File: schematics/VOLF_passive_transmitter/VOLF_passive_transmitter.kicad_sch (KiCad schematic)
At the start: 7 parts, among them J1 AudioJack3, Q1 IRF3205

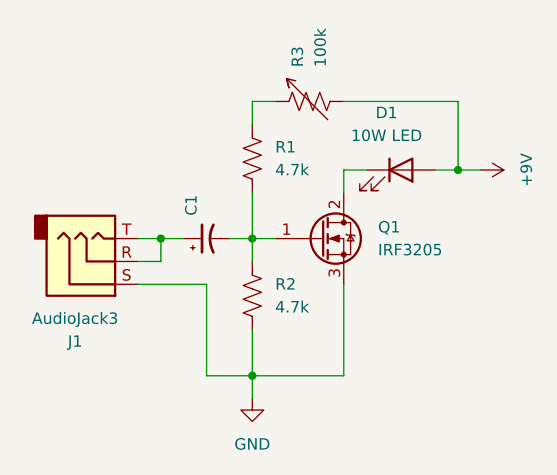
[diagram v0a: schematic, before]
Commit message: added documentation for passive circuits
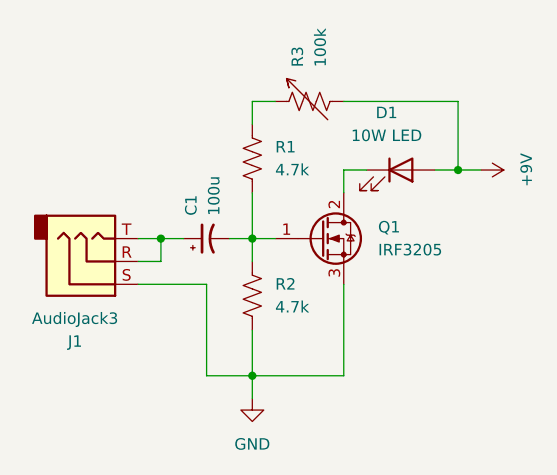
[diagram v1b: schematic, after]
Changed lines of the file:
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@@
 				)
 				(justify left)
-				(hide yes)
 			)
 		)
